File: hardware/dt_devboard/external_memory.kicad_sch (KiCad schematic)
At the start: 1 part, among them U1 AT25FF041A-SSHN-T

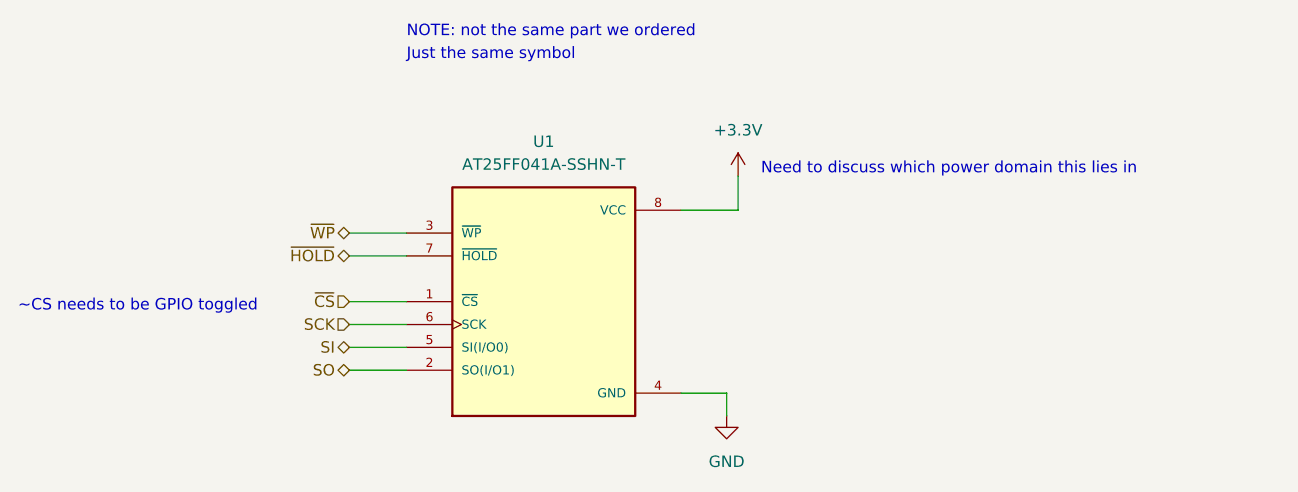
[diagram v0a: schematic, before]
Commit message: adding software packages
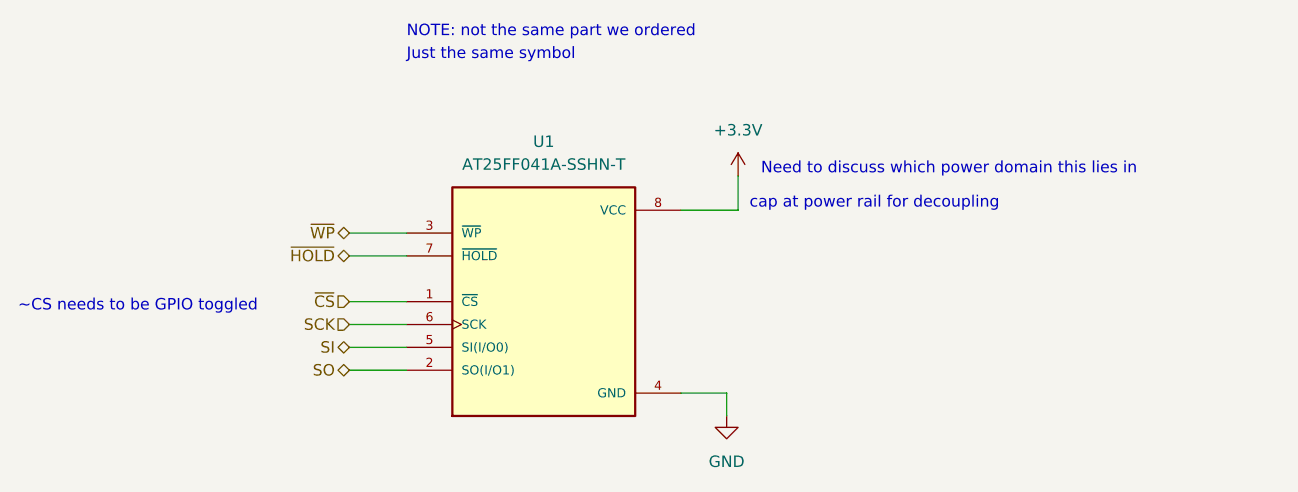
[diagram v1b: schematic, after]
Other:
- note added: "cap at power rail for decoupling"
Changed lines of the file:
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@@
+    (effects (font (size 1.27 1.27)) (justify left bottom))
+  )
+  (text "cap at power rail for decoupling" (at 111.76 52.07 0)
     (effects (font (size 1.27 1.27)) (justify left bottom))
   )
